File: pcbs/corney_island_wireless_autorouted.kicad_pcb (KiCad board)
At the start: 2 copper layers, 133.8 x 91.7 mm, 75 parts

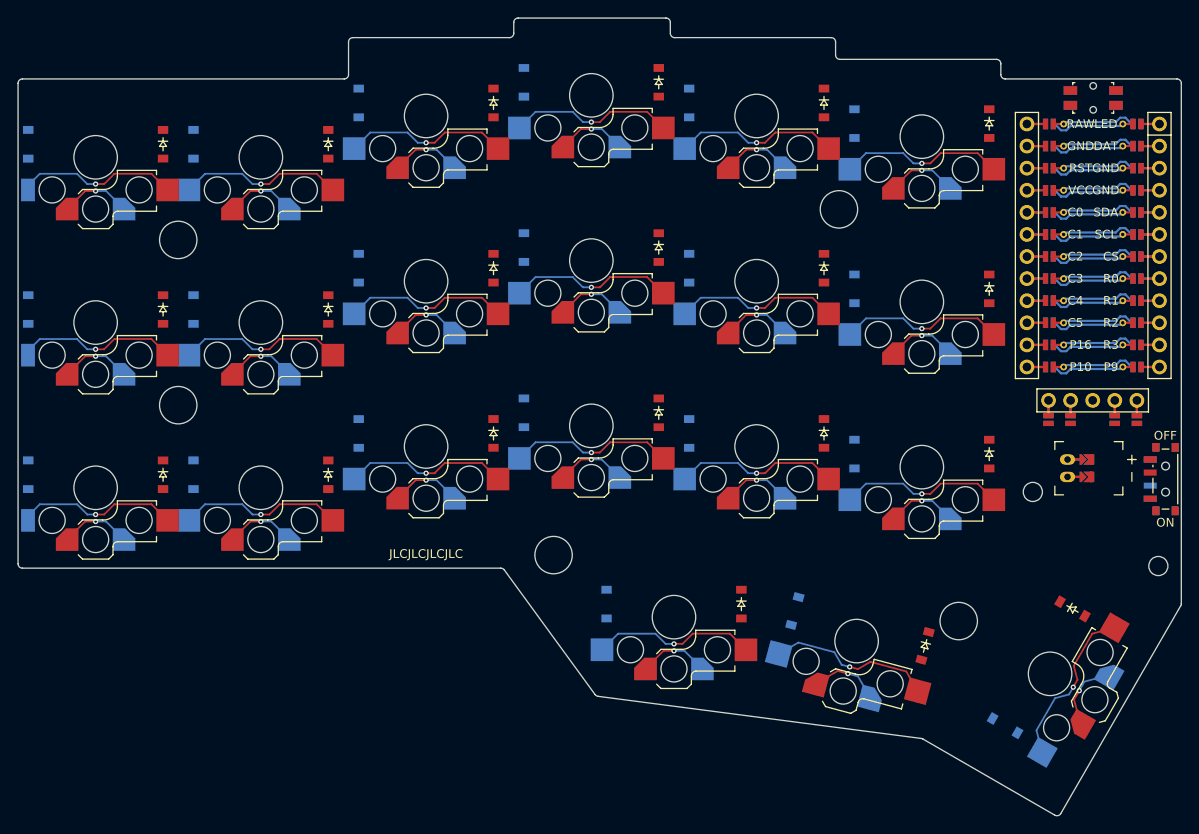
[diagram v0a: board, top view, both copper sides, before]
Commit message: build: generate PCB layouts, routing, gerbers, and preview images
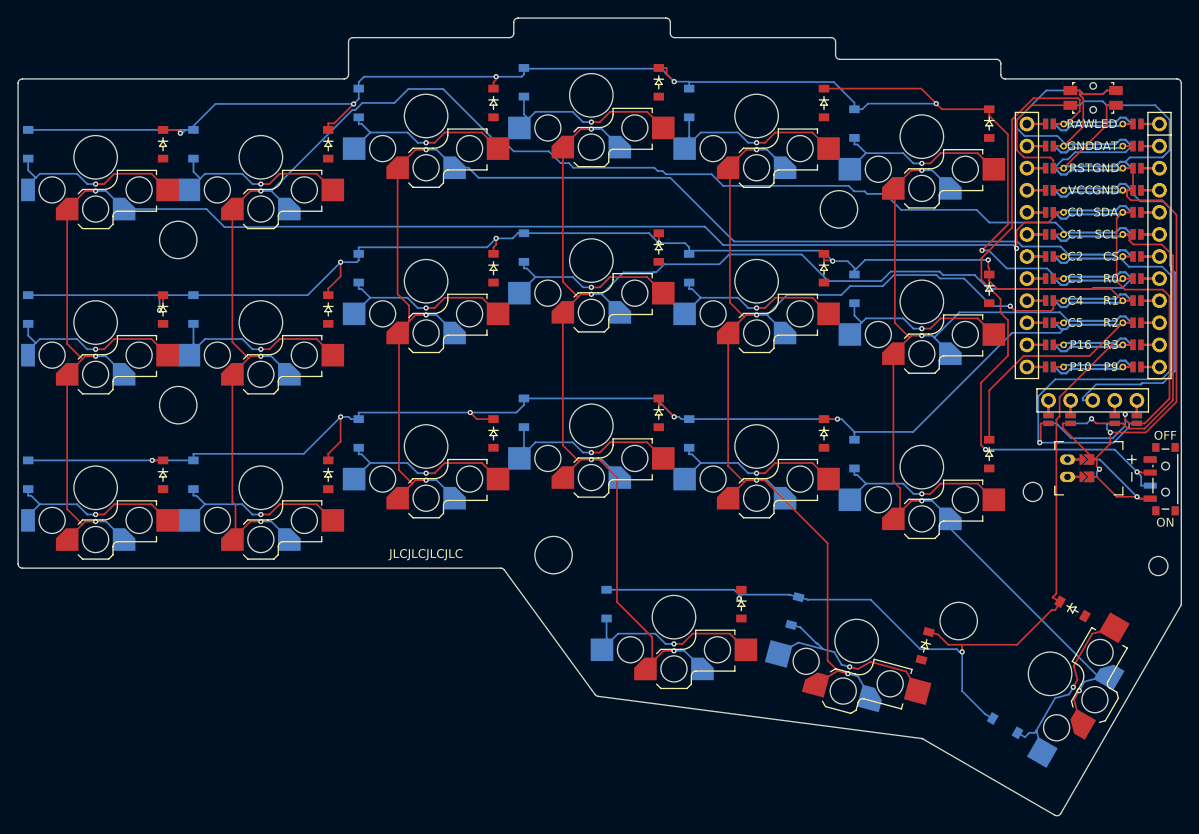
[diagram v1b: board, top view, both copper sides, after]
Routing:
- net R0: track 9.63 -> 182.6 mm, vias 0 -> 6
- net R2: track 9.63 -> 179.6 mm, vias 0 -> 5
- net R1: track 9.63 -> 159.4 mm, vias 0 -> 6
- net C0: track 34.5 -> 183.0 mm, vias 3 -> 4
- net C1: track 34.5 -> 175.0 mm
- net C3: track 42.7 -> 171.5 mm
- net C2: track 34.5 -> 145.8 mm
- net R3: track 9.63 -> 117.2 mm, vias 0 -> 2
- net GND: track 28.9 -> 129.8 mm, vias 0 -> 2
- net C4: track 42.7 -> 143.3 mm, vias 4 -> 5
- net C5: track 42.7 -> 122.9 mm
- net RAW: track 9.64 -> 87.6 mm, vias 0 -> 2
- net CS: track 9.63 -> 64.9 mm, vias 0 -> 1
- net RST: track 9.64 -> 57.9 mm
- net SDA: track 9.63 -> 55.2 mm, vias 0 -> 1
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
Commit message: build: regenerate PCBs, images, and gerbers
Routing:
- net C0: track 183.0 -> 34.8 mm, vias 4 -> 3
- net C1: track 175.0 -> 34.8 mm
- net C2: track 145.8 -> 34.8 mm
- net C4: track 143.3 -> 43.0 mm, vias 5 -> 4
- net C3: track 171.5 -> 89.4 mm, vias 4 -> 5
- net C5: track 122.9 -> 43.0 mm
- net R2: track 179.6 -> 152.8 mm, vias 5 -> 6
- net GND: track 129.8 -> 103.4 mm
- net RAW: track 87.6 -> 62.1 mm
- net RST: track 57.9 -> 40.0 mm, vias 0 -> 2
- net VCC: track 48.3 -> 35.6 mm
- net R0: track 182.6 -> 171.9 mm
- net CS: track 64.9 -> 57.8 mm, vias 1 -> 2
- net mid_home_B: track 25.2 -> 22.0 mm
- net SDA: track 55.2 -> 52.2 mm
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
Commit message: fix(build): restore NPTH normalization and regenerate boards
Normalize source-proven NPTH export obstacles by default, with a native-export opt-out. Pin and verify Freerouting 2.5.1-SNAPSHOT at upstream head 1be66ad and use KiCad 9 for generation, import, and DRC. Make CI run the same build and withhold stale or failing fabrication outputs.

Regenerate the keyboard boards and plates from YAML, including the configured rectangular JST jumpers. Retain routed review boards and unfiltered validation evidence: wireless has one open C4 connection; wired has two open VCC connections. Routing introduces no new KiCad DRC errors. Existing LED clearance and frontplate outline findings remain documented.

Validation: 17 regression tests, actual KiCad 9 export preservation and idempotence checks, post-import DRC, 100 um track-width floor, ShellCheck, shell syntax, workflow YAML validation, and git diff --check.
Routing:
- net C0: track 34.8 -> 188.4 mm
- net C1: track 34.8 -> 164.2 mm
- net C2: track 34.8 -> 148.6 mm
- net C5: track 43.0 -> 122.1 mm
- net C3: track 89.4 -> 164.3 mm
- net C4: track 43.0 -> 117.5 mm
- net GND: track 103.4 -> 137.4 mm
- net R0: track 171.9 -> 162.6 mm, vias 6 -> 7
- net R3: track 116.1 -> 124.8 mm, vias 3 -> 2
- net RST: track 40.0 -> 45.4 mm, vias 2 -> 0
- net R1: track 159.1 -> 153.7 mm, vias 6 -> 8
- net R2: track 152.8 -> 157.4 mm
- net CS: track 57.8 -> 53.9 mm, vias 2 -> 1
- net BAT_P: track 13.7 -> 17.6 mm, vias 2 -> 1
- net RAW: track 62.1 -> 58.9 mm
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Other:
- rule pad_to_mask_clearance: 0.05 -> 0

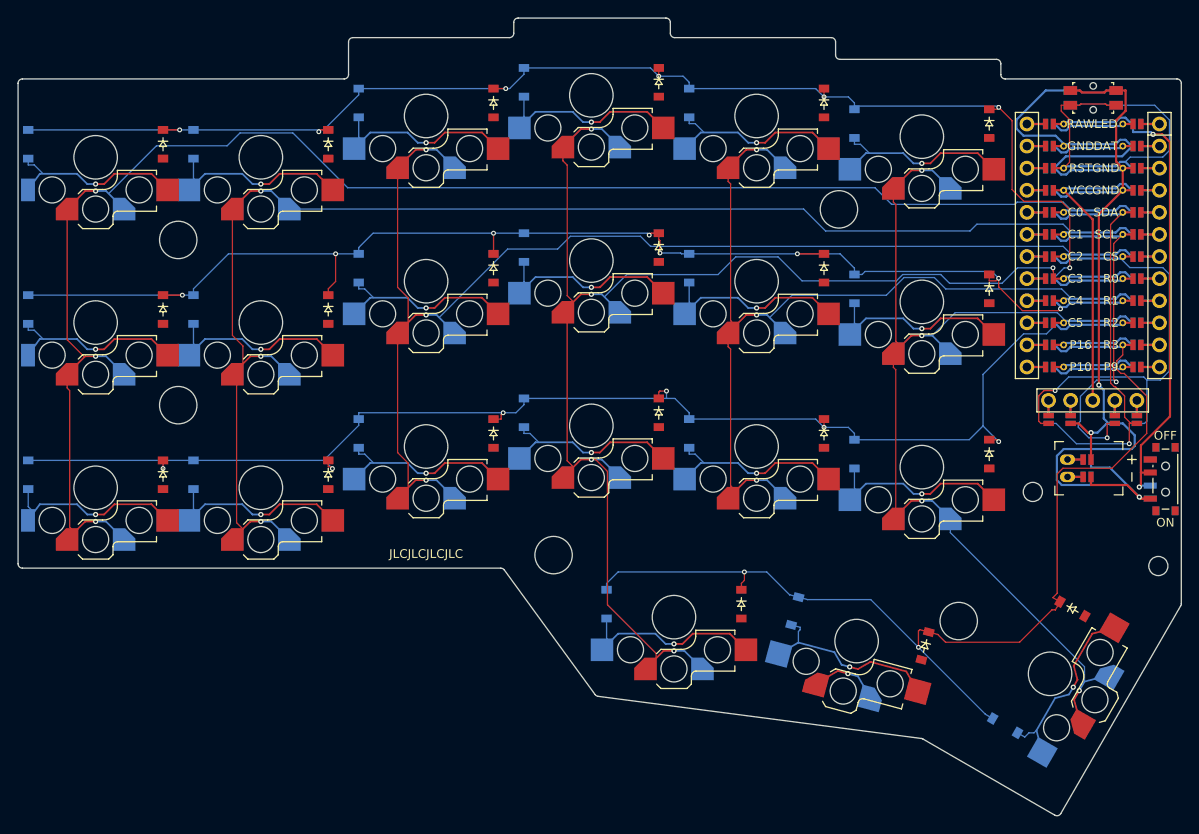
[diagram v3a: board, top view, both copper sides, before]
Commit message: Refresh generated Corney Island boards and KiCad projects
Regenerate with KiCad 9.0.7+1 and the Freerouting fixes at 48c969dd, using
neckdown and fanout disabled, one worker, and optimization enabled. The fixed
JAR was mounted over the pinned image for this local build.

Both boards have zero missing connections after SES import. Wireless has no
DRC errors; wired retains the 16 source copper-edge errors. The frontplate
still fails its outline check, so failed-board fabrication exports are skipped.

Regenerate wireless fabrication outputs after the unfiltered KiCad DRC passes,
bypassing KiBot's subsequent HTML-report parsing failure. Include the generated
project settings with the boards, reports, images, and archives.
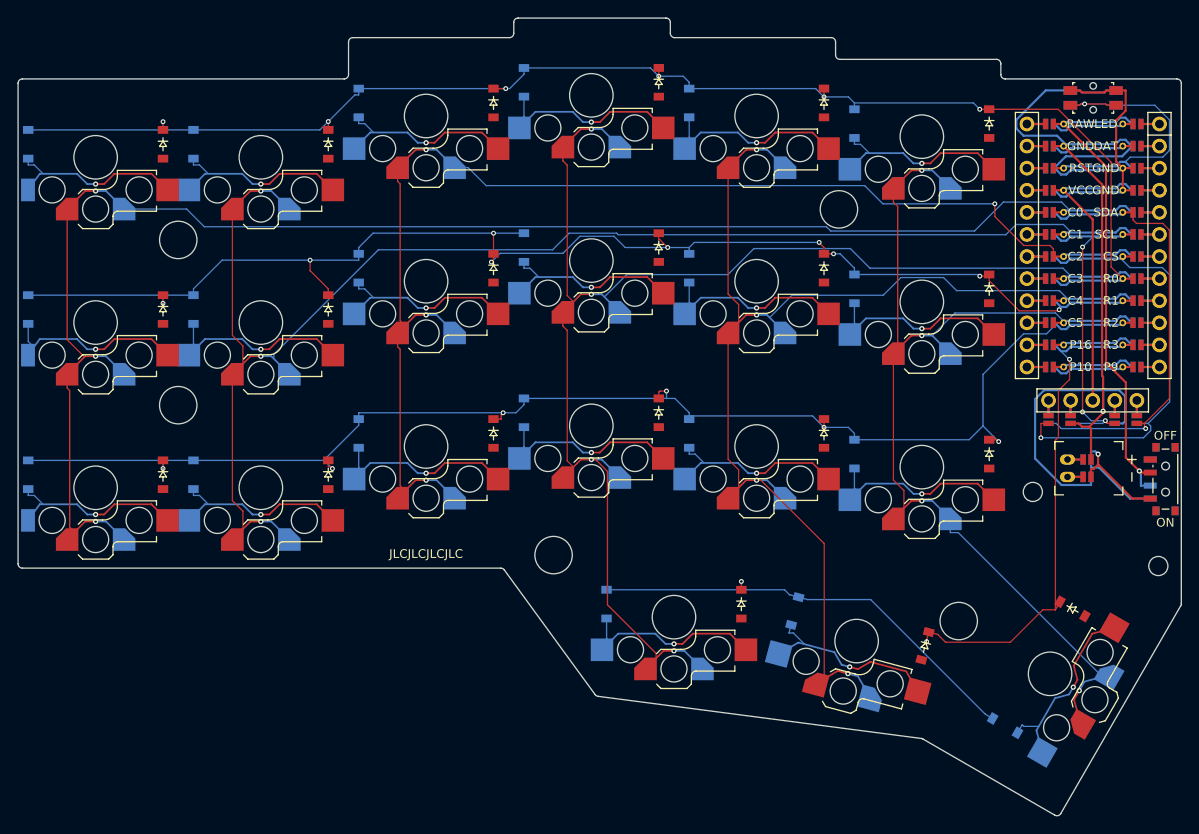
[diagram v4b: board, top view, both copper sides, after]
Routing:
- net C4: track 117.5 -> 142.9 mm
- net GND: track 137.4 -> 152.6 mm, vias 2 -> 1
- net R3: track 124.8 -> 112.7 mm, vias 2 -> 3
- net RST: track 45.4 -> 36.5 mm, vias 0 -> 1
- net C1: track 164.2 -> 170.1 mm
- net C0: track 188.4 -> 182.5 mm
- net BAT_P: track 17.6 -> 21.9 mm
- net SCL: track 43.1 -> 38.9 mm, vias 2 -> 3
- net SDA: track 49.1 -> 52.5 mm
- net R1: track 153.7 -> 156.4 mm, vias 8 -> 9
- net C2: track 148.6 -> 146.0 mm, vias 3 -> 4
- net CS: track 53.9 -> 52.0 mm
- net RAW: track 58.9 -> 57.4 mm, vias 2 -> 1
- net C3: track 164.3 -> 163.0 mm, vias 5 -> 4
- net R0: track 162.6 -> 163.8 mm, vias 7 -> 6
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
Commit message: Update LED footprint clearance and refresh generated boards
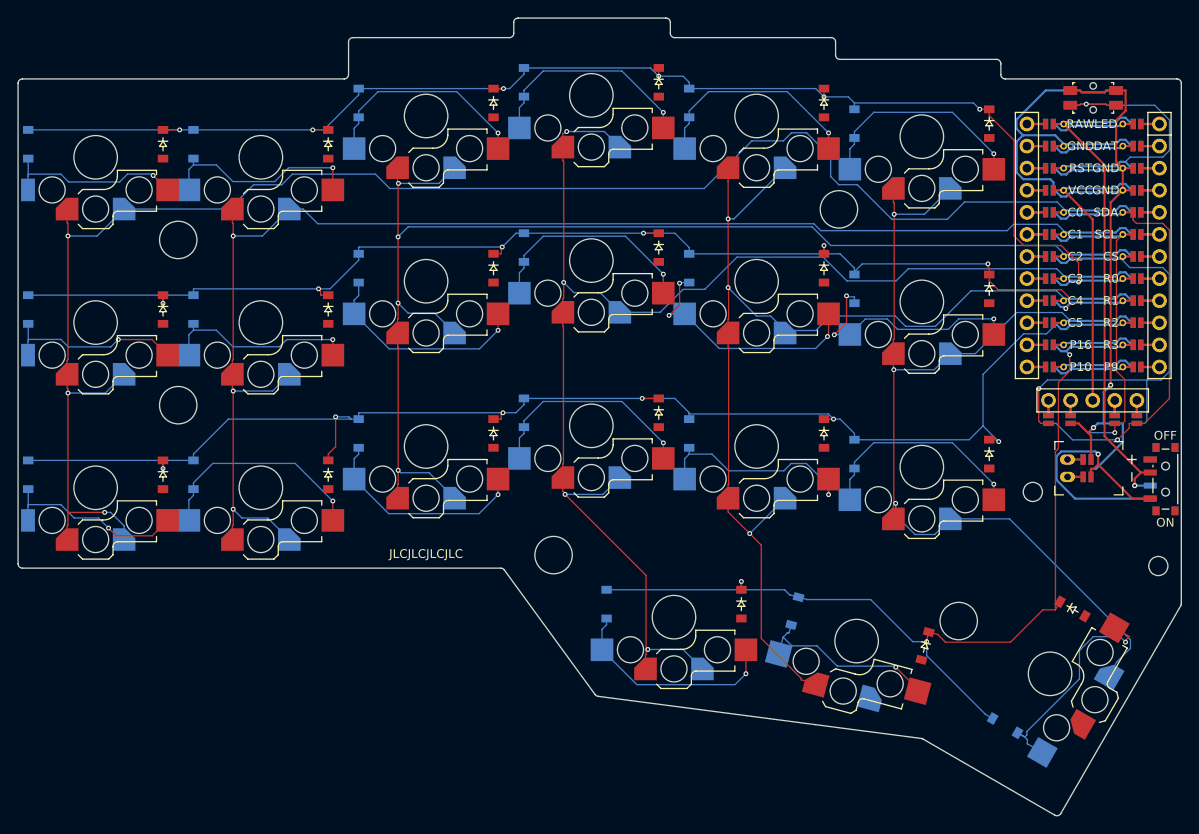
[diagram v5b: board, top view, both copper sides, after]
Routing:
- net GND: track 152.6 -> 124.5 mm, vias 1 -> 2
- net C4: track 142.9 -> 133.0 mm, vias 4 -> 3
- net BAT_P: track 21.9 -> 31.2 mm
- net C0: track 182.5 -> 191.6 mm
- net C1: track 170.1 -> 161.8 mm
- net inner_home_B: track 21.9 -> 28.6 mm, vias 1 -> 3
- net index_home_B: track 21.9 -> 28.5 mm, vias 1 -> 3
- net R1: track 156.4 -> 150.1 mm, vias 9 -> 7
- net far_home_B: track 22.1 -> 26.4 mm
- net R2: track 157.6 -> 161.8 mm
- net pinky_bottom_B: track 21.9 -> 25.5 mm
- net middle_home_B: track 21.9 -> 25.5 mm
- net near_home_B: track 21.9 -> 25.3 mm
- net index_top_B: track 21.9 -> 25.3 mm
- net inner_bottom_B: track 21.9 -> 25.3 mm
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
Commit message: Bump version to 0.4 and updated artifacts
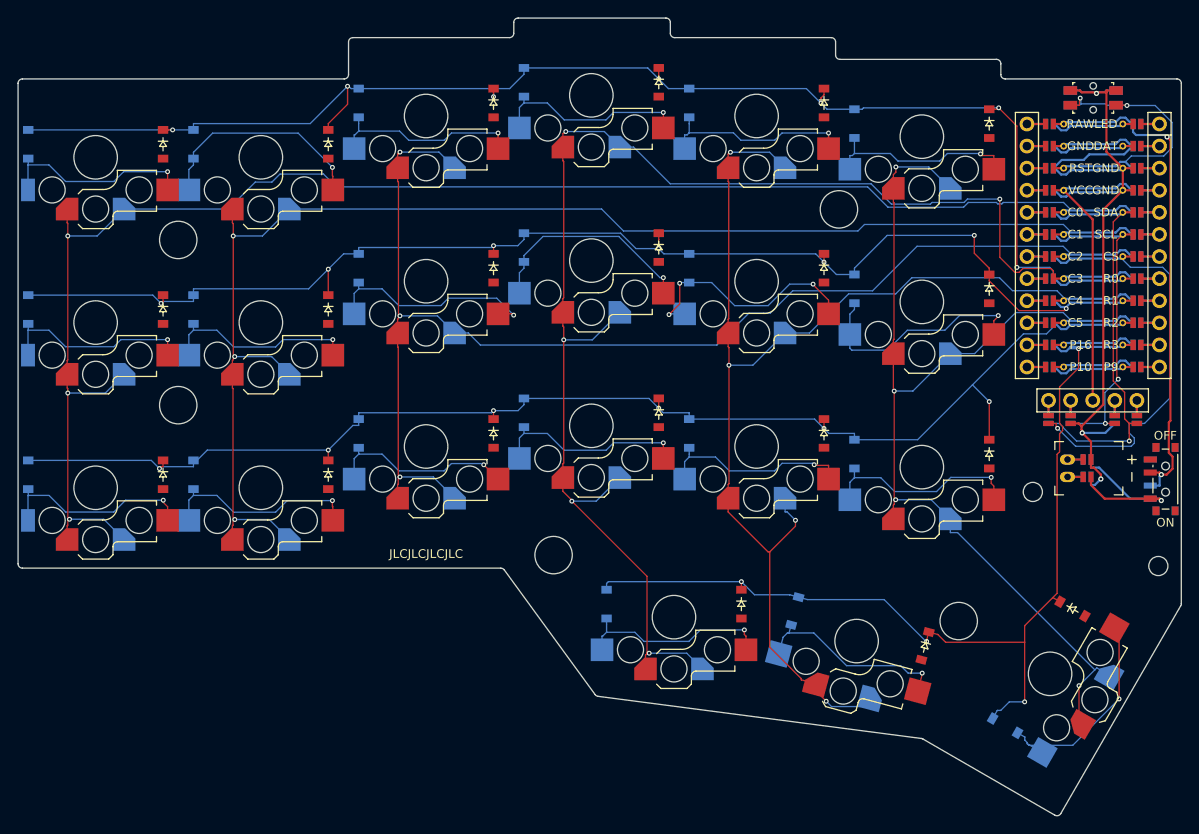
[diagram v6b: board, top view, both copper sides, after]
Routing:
- net GND: track 124.5 -> 106.8 mm, vias 2 -> 3
- net BAT_P: track 31.2 -> 20.4 mm
- net C4: track 133.0 -> 143.2 mm, vias 3 -> 4
- net C0: track 191.6 -> 183.4 mm
- net R2: track 161.8 -> 154.6 mm
- net C3: track 161.2 -> 165.9 mm, vias 4 -> 5
- net CS: track 54.1 -> 50.0 mm
- net R0: track 161.5 -> 165.0 mm
- net C5: track 119.9 -> 123.4 mm, vias 3 -> 4
- net SDA: track 51.6 -> 48.3 mm
- net ring_bottom_B: track 24.7 -> 21.7 mm
- net inner_top_B: track 25.2 -> 22.4 mm
- net ring_top_B: track 25.3 -> 22.5 mm
- net index_top_B: track 25.3 -> 22.5 mm
- net middle_top_B: track 25.2 -> 22.8 mm
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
